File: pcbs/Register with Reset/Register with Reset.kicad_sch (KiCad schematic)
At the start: 1 part, among them J101 Conn_02x20_Odd_Even

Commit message: Adding design rules
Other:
- title: (none) -> 16-bit Register with Reset
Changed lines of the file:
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@@
 	(generator_version "8.0")
 	(paper "A4")
+	(title_block
+		(title "16-bit Register with Reset")
+		(rev "0")
+	)
 	(junction
 		(at 73.66 68.58)

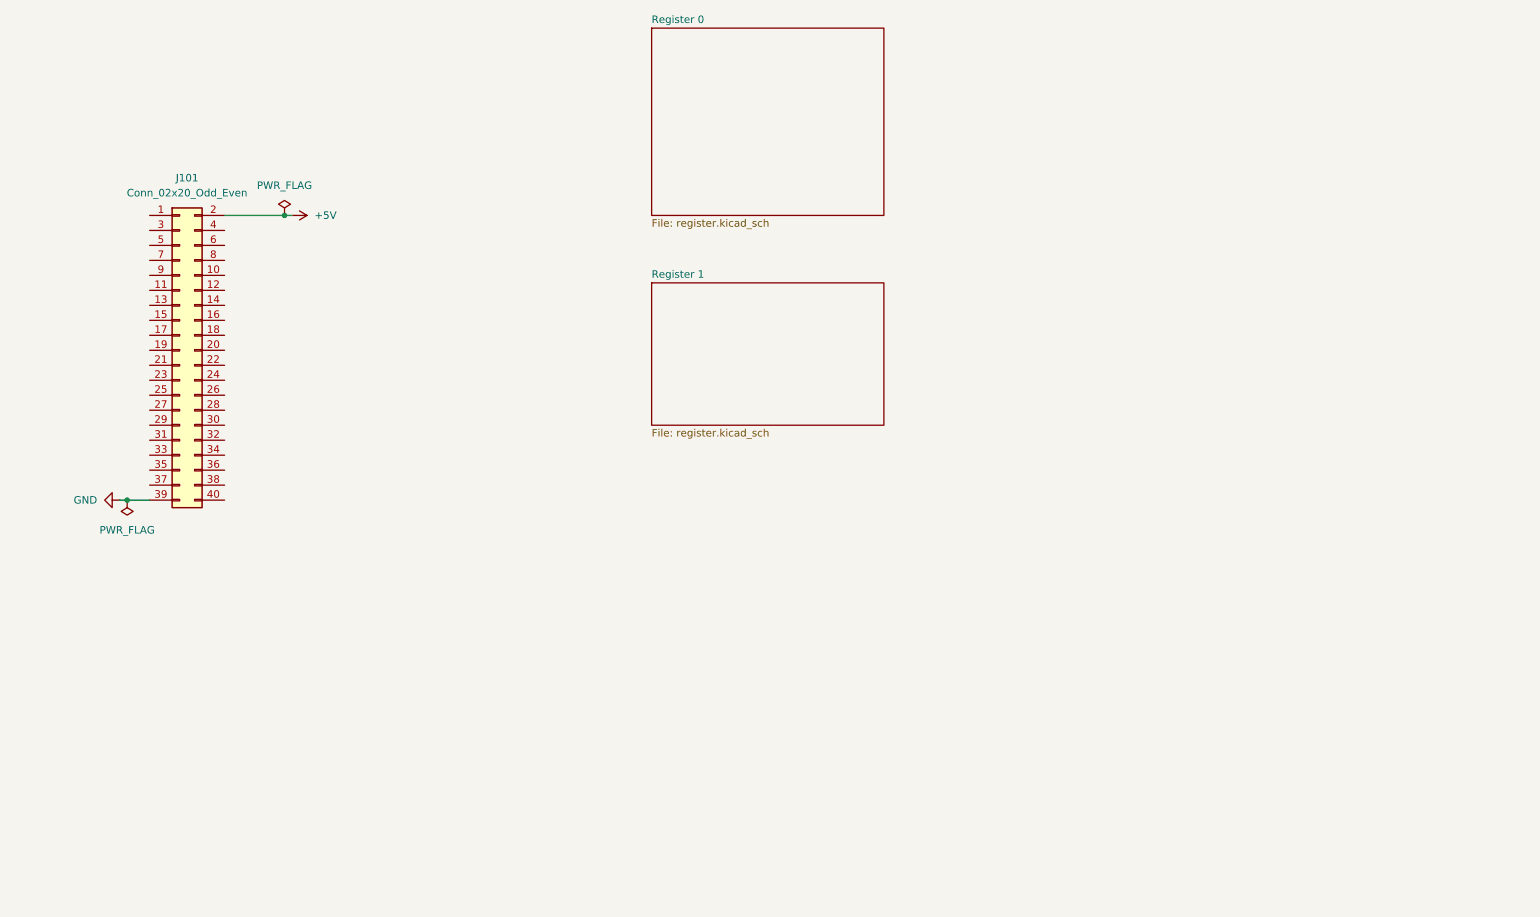
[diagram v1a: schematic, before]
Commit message: Routing the actual registers
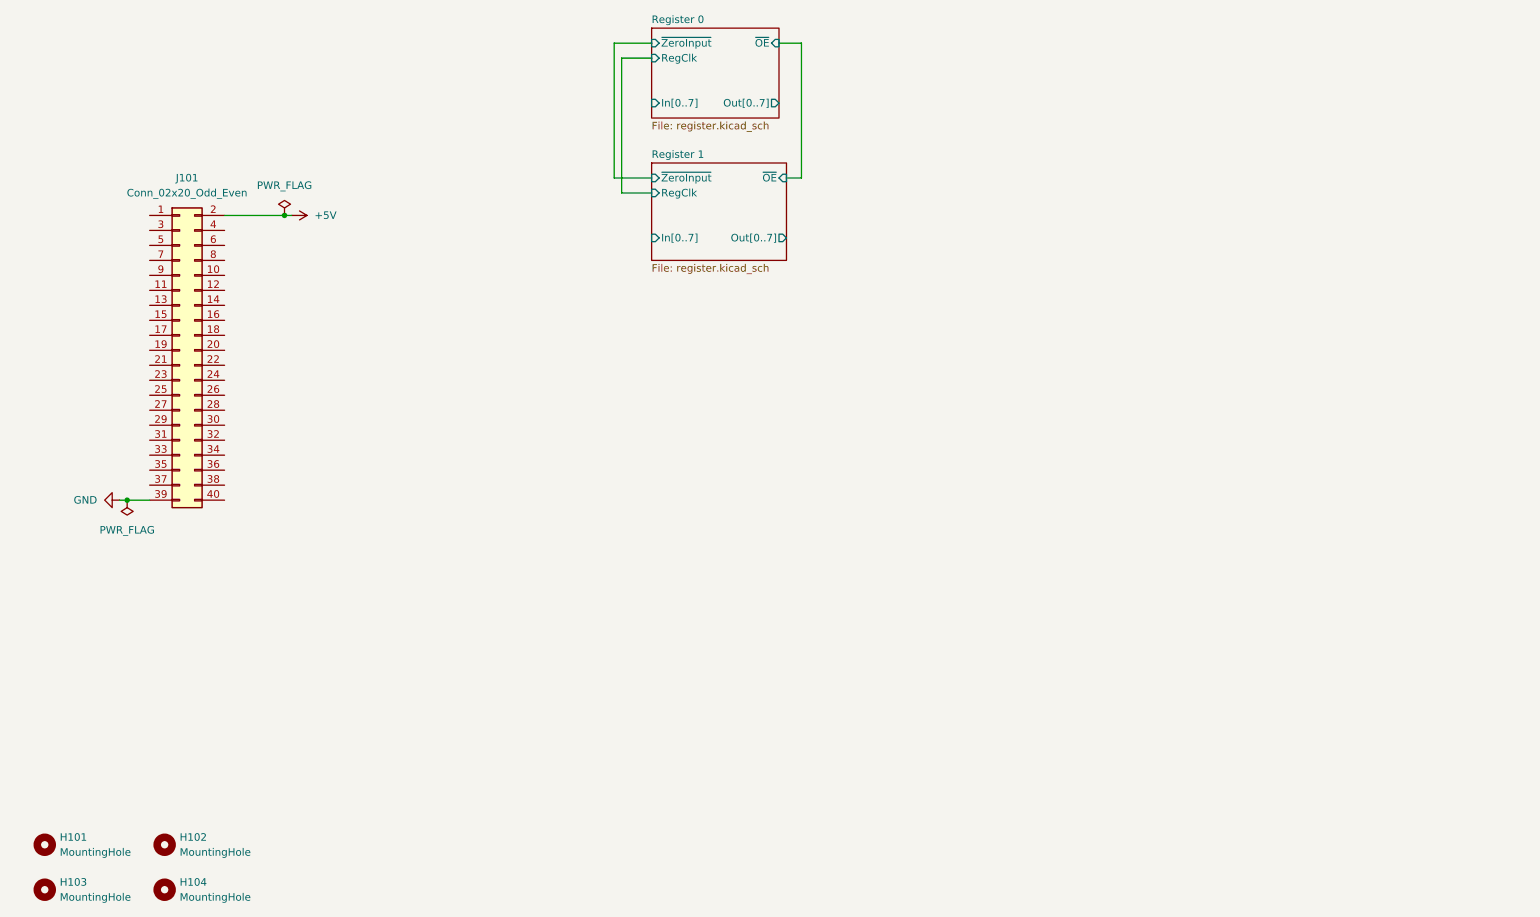
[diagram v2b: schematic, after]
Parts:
- added H101, H102, H103, H104: MountingHole, MountingHole:MountingHole_3mm, symbol Mechanical:MountingHole
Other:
- sheet Register 0 ports: added In[0..7], Out[0..7], RegClk, ~{OE}, ~{ZeroInput}; removed none
- sheet Register 1 ports: added In[0..7], Out[0..7], RegClk, ~{OE}, ~{ZeroInput}; removed none

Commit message: Working on reset logic and some routing
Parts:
- H101, H102, H103, H104: footprint MountingHole:MountingHole_3mm -> MountingHole:MountingHole_2.7mm_M2.5
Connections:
- net Reg0.In7: now reaches J101.10 (Pin_10)
- net Reg1.In0: now reaches J101.11 (Pin_11)
- net Reg1.In1: now reaches J101.12 (Pin_12)
- net Reg1.In2: now reaches J101.13 (Pin_13)
- net Reg1.In3: now reaches J101.14 (Pin_14)
- net Reg1.In4: now reaches J101.15 (Pin_15)
- net Reg1.In5: now reaches J101.16 (Pin_16)
- net Reg1.In6: now reaches J101.17 (Pin_17)
- net Reg1.In7: now reaches J101.18 (Pin_18)
- net Reg0.Out0: now reaches J101.23 (Pin_23)
- net Reg0.Out1: now reaches J101.24 (Pin_24)
- net Reg0.Out2: now reaches J101.25 (Pin_25)
- net Reg0.Out3: now reaches J101.26 (Pin_26)
- net Reg0.Out4: now reaches J101.27 (Pin_27)
- net Reg0.Out5: now reaches J101.28 (Pin_28)
- net Reg0.Out6: now reaches J101.29 (Pin_29)
- net Reg0.In0: now reaches J101.3 (Pin_3)
- net Reg0.Out7: now reaches J101.30 (Pin_30)
- net Reg1.Out0: now reaches J101.31 (Pin_31)
- net Reg1.Out1: now reaches J101.32 (Pin_32)
- net Reg1.Out2: now reaches J101.33 (Pin_33)
- net Reg1.Out3: now reaches J101.34 (Pin_34)
- net Reg1.Out4: now reaches J101.35 (Pin_35)
- net Reg1.Out5: now reaches J101.36 (Pin_36)
- net Reg1.Out6: now reaches J101.37 (Pin_37)
- net Reg1.Out7: now reaches J101.38 (Pin_38)
- net Reg0.In1: now reaches J101.4 (Pin_4)
- net Reg0.In2: now reaches J101.5 (Pin_5)
- net Reg0.In3: now reaches J101.6 (Pin_6)
- net Reg0.In4: now reaches J101.7 (Pin_7)
- net Reg0.In5: now reaches J101.8 (Pin_8)
- net Reg0.In6: now reaches J101.9 (Pin_9)
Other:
- added sheet ResetLogic (resetlogic.kicad_sch)

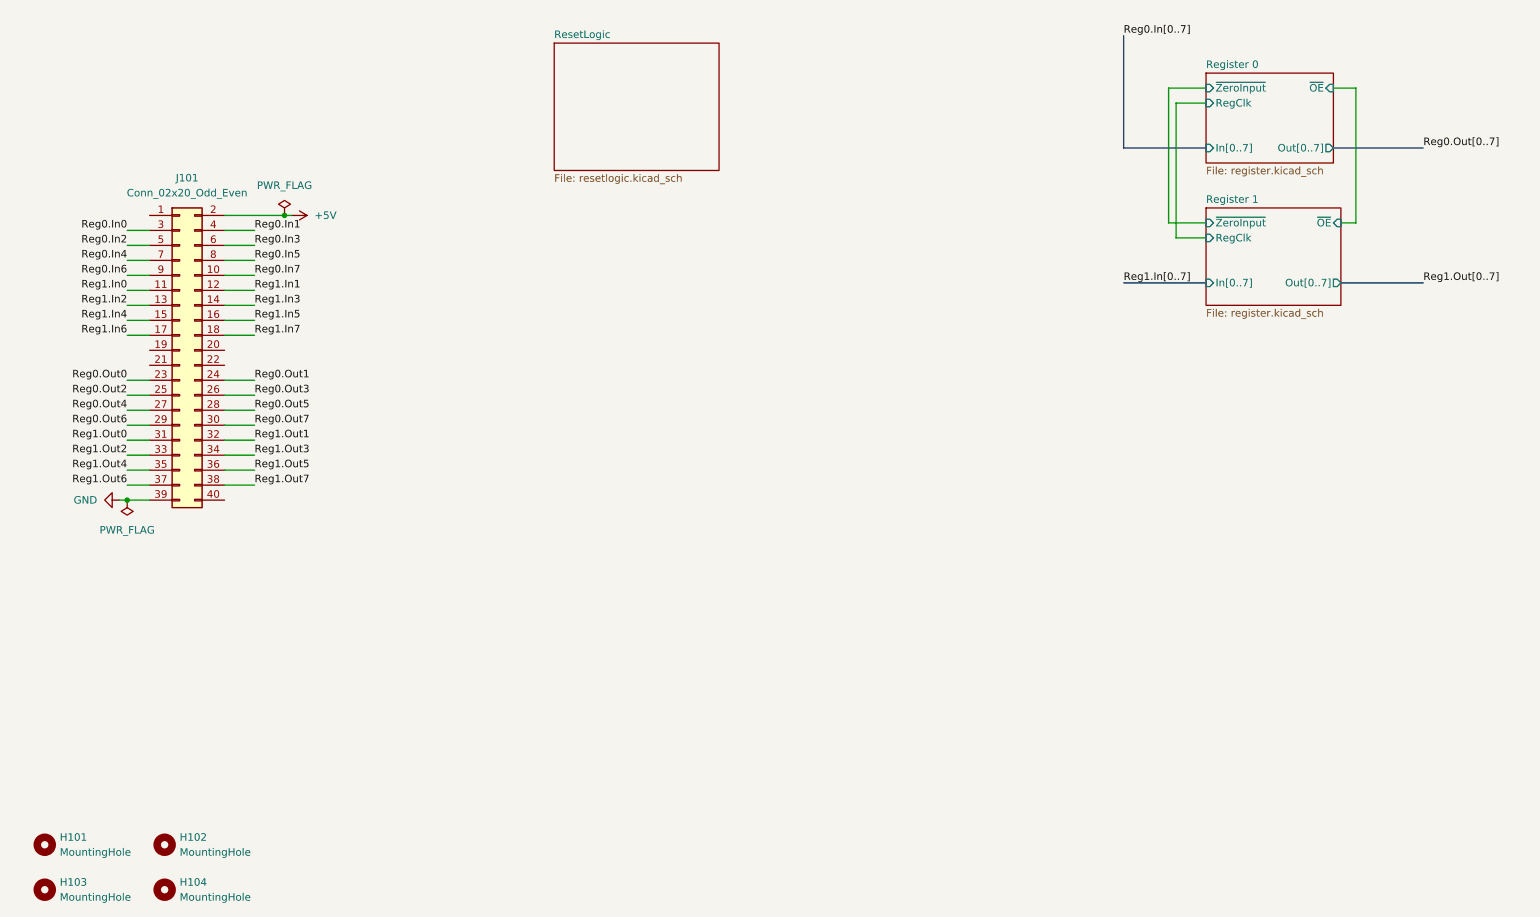
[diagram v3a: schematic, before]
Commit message: First draft of whole board
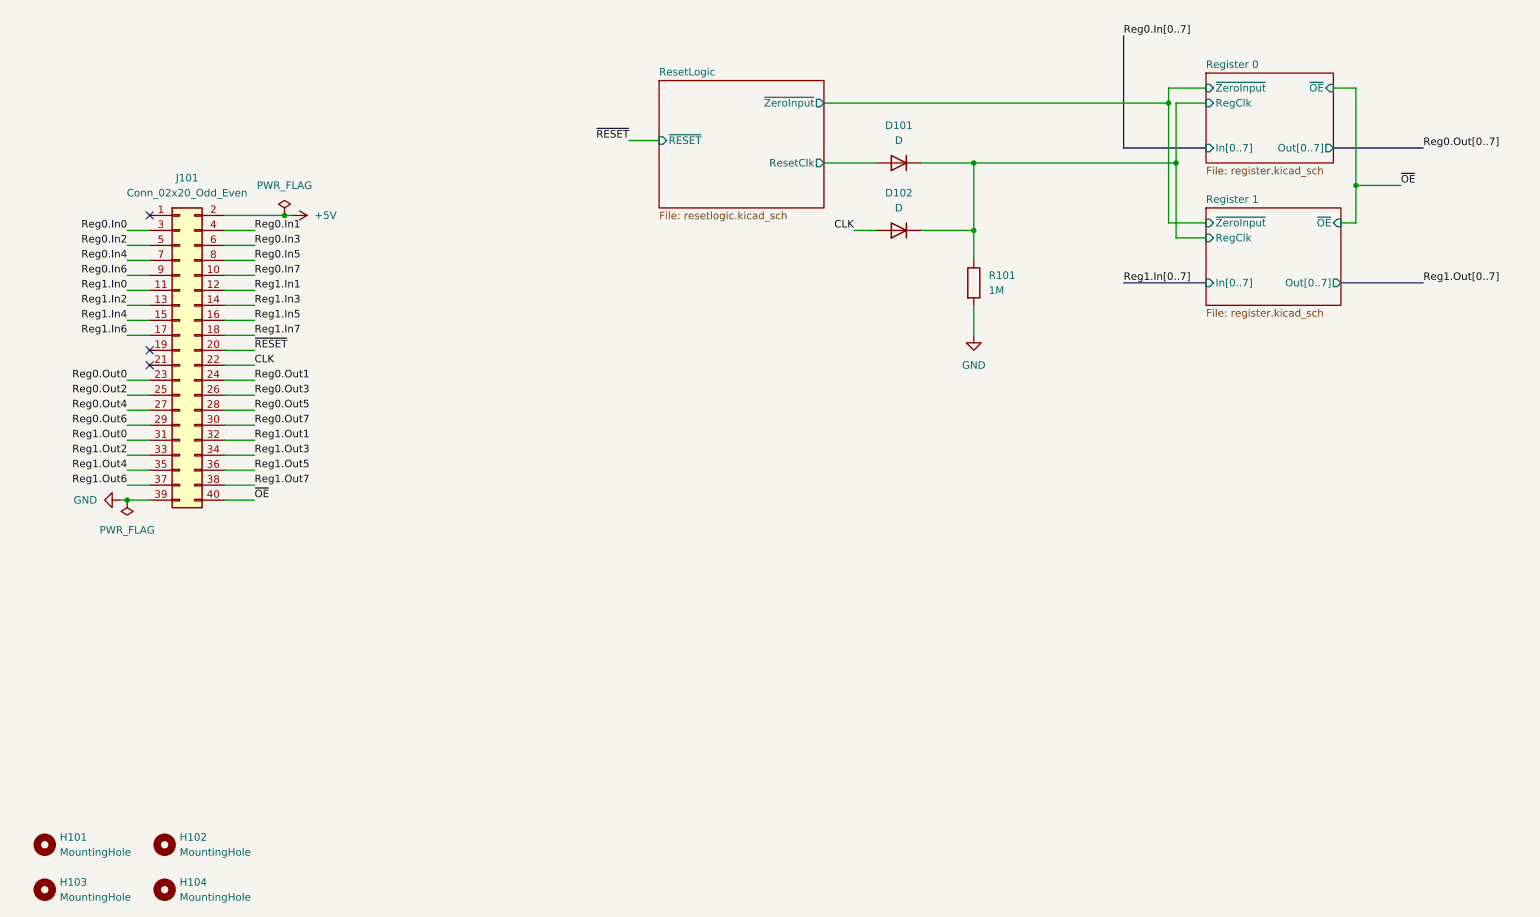
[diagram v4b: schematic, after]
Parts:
- added D101, D102: D, Diode_SMD:D_SOD-123, symbol Device:D
- added R101: 1M, Resistor_SMD:R_0603_1608Metric, symbol Device:R
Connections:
- net GND: now also R101.2
- net Register 0/RegClk: now also D101.1 (K), D102.1 (K), R101.1
- net ~{RESET}: now reaches J101.20 (Pin_20)
- net CLK: now reaches J101.22 (Pin_22)
- net CLK: now also D102.2 (A)
- net ~{OE}: now reaches J101.40 (Pin_40)
- new net ResetLogic/ResetClk: D101.2 (A)
- no-connect marks 0 -> 3
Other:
- sheet ResetLogic ports: added ResetClk, ~{RESET}, ~{ZeroInput}; removed none

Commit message: Fix the reset logic....
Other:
- sheet Register 0 ports: added ZeroInput; removed ~{ZeroInput}
- sheet Register 1 ports: added ZeroInput; removed ~{ZeroInput}
- sheet ResetLogic ports: added ZeroInput; removed ~{ZeroInput}

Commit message: Revise the Register with Reset (#3)
Updates to Register-with-Reset:

- Convert to edge connector
- Route clock through an 'AND' with the Reset line, so the clock doesn't block reset
- Shrink the board somewhat by repositioning components
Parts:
- removed H101, H102, H103, H104: MountingHole, MountingHole:MountingHole_2.7mm_M2.5, symbol Mechanical:MountingHole
- removed J101: Conn_02x20_Odd_Even, Connector_IDC:IDC-Header_2x20_P2.54mm_Vertical, symbol Connector_Generic:Conn_02x20_Odd_Even
- added J101: ~, BoardEdgeConnectors:TE-5530843-4-Edge, symbol BoardEdgeConnectors:TE-5530843-4
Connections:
- net +5V: now also J101.B1
- net CLK: now also J101.B11; no longer D102.2 (A)
- net GND: now also J101.A22
- net Reg0.In0: now also J101.A2
- net Reg0.In1: now also J101.B2
- net Reg0.In2: now also J101.A3
- net Reg0.In3: now also J101.B3
- net Reg0.In4: now also J101.A4
- net Reg0.In5: now also J101.B4
- net Reg0.In6: now also J101.A5
- net Reg0.In7: now also J101.B5
- net Reg0.Out0: now also J101.A12
- net Reg0.Out1: now also J101.B12
- net Reg0.Out2: now also J101.A13
- net Reg0.Out3: now also J101.B13
- net Reg0.Out4: now also J101.A14
- net Reg0.Out5: now also J101.B14
- net Reg0.Out6: now also J101.A15
- net Reg0.Out7: now also J101.B15
- net Reg1.In0: now also J101.A6
- net Reg1.In1: now also J101.B6
- net Reg1.In2: now also J101.A7
- net Reg1.In3: now also J101.B7
- net Reg1.In4: now also J101.A8
- net Reg1.In5: now also J101.B8
- net Reg1.In6: now also J101.A9
- net Reg1.In7: now also J101.B9
- net Reg1.Out0: now also J101.A16
- net Reg1.Out1: now also J101.B16
- net Reg1.Out2: now also J101.A17
- net Reg1.Out3: now also J101.B17
- net Reg1.Out4: now also J101.A18
- net Reg1.Out5: now also J101.B18
- net Reg1.Out6: now also J101.A19
- net Reg1.Out7: now also J101.B19
- net ~{OE}: now also J101.B20
- net ~{RESET}: now also J101.B10
- new net ResetLogic/CLK_{Out}: D102.2 (A)
- no-connect marks 3 -> 7
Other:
- sheet ResetLogic ports: added CLK_{Out}, CLK_{in}; removed none
